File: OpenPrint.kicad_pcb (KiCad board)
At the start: 2 copper layers, 20 x 20 mm, 46 parts, among them IC1 SN74AHCT1G125, IC2 100026223, J1 USB4215-03-A_REVA, U1 RP2354A, U2 AP2112K-3.3, U3 ATECC608C-MAHDA, U4 USBLC6-2SC6, Y1 ABM8-272-T3

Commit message: initial layout done
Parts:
- removed JP1, JP2: Jumper_2_Open, TestPoint:TestPoint_2Pads_Pitch2.54mm_Drill0.8mm
- removed the R12 at (123.0, 59.5)
- added C19: 0.1uF, Capacitor_SMD:C_0402_1005Metric, F.Cu at (98.5, 60.5)
- added D2: WS2812B-2020, LED_SMD:LED_WS2812B-2020_PLCC4_2.0x2.0mm, B.Cu at (99.5, 60.5)
- added H1: MountingHole_Pad, MountingHole:MountingHole_2.2mm_M2_Pad, F.Cu at (100.5, 50.5)
- added H2: MountingHole_Pad, MountingHole:MountingHole_2.2mm_M2_Pad, F.Cu at (119.5, 50.5)
- added H3: MountingHole, MountingHole:MountingHole_2mm, F.Cu at (100.5, 69.5)
- added H4: MountingHole, MountingHole:MountingHole_2mm, F.Cu at (119.5, 69.5)
- added R14: 5.1k, Resistor_SMD:R_0402_1005Metric, B.Cu at (117.5, 54.5)
- added S1: SKRPABE010, SamacSys_Parts:SW_SKRPABE010, B.Cu at (120.5, 56.0)
- added S2: SKRPABE010, SamacSys_Parts:SW_SKRPABE010, B.Cu at (99.5, 56.0)
- C1: renamed from C23; moved to B.Cu
- C10: renamed from C9; moved to B.Cu
- C11, C13, C15, C21, C8, IC1, L1, R1, R13, R2, R3, R4, R5, Y1: moved to B.Cu
- C12: renamed from C10; moved to B.Cu
- C14: renamed from C12; moved to B.Cu
- C16: renamed from C17; moved to B.Cu
- C2: renamed from C3; moved to B.Cu
- C20: renamed from C19; moved to B.Cu
- C3: renamed from C1; moved to B.Cu
- C4: renamed from C2; moved to B.Cu
- C5: renamed from C4; moved to B.Cu
- C6: renamed from C5; moved to B.Cu
- C7: renamed from C6; moved to B.Cu
- C9: renamed from C7; moved to B.Cu
- D1: value WS2812B -> WS2812B-2020; footprint LED_SMD:LED_WS2812B_PLCC4_5.0x5.0mm_P3.2mm -> LED_SMD:LED_WS2812B-2020_PLCC4_2.0x2.0mm; moved to B.Cu
- J1: value USB4215-03-A_REVA -> USB4110; footprint SamacSys_Parts:GCT_USB4215-03-A_REVA -> Connector_USB:USB_C_Receptacle_GCT_USB4110
- R6: renamed from R9; moved to B.Cu
- R7: renamed from R6; moved to B.Cu
- R8: renamed from R7; moved to B.Cu
- R9: renamed from R8; moved to B.Cu
- U1: renamed from U3; moved to B.Cu
- U2: renamed from U1; moved to B.Cu
- U3: renamed from U4; moved to B.Cu
- U4: renamed from U2; moved to B.Cu
- moved R6 37.8 mm to (93.0, 52.0), turned to -90 degrees
- moved U1 30.2 mm to (104.0, 59.0), turned to 90 degrees
- moved U2 25.9 mm to (110.0, 65.0), turned to -90 degrees
- moved R8 25.6 mm to (102.0, 56.5), turned to -90 degrees
- moved R9 25.5 mm to (102.0, 58.5), turned to 90 degrees
- moved C17 25.4 mm to (98.5, 64.0), turned to 90 degrees
- moved IC1 25.0 mm to (100.5, 64.5), turned to 180 degrees
- moved D1 24.9 mm to (120.5, 60.5), turned to 180 degrees
- moved L1 23.9 mm to (103.0, 68.1), turned to -90 degrees
- moved R13 21.6 mm to (102.5, 54.5), turned to -90 degrees
- moved C20 21.4 mm to (115.5, 56.5)
- moved R12 21.3 mm to (118.5, 61.5), turned to -90 degrees
- moved C21 20.5 mm to (115.0, 61.5)
- moved R11 20.4 mm to (118.5, 58.5), turned to 90 degrees
- moved C1 20.3 mm to (106.0, 58.0), turned to 90 degrees
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- renumbered C14 to C17, C16 to C18, R14 to R10, R10 to R11, R11 to R12
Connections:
- D1 pad 1: VBUS -> Net-(D1-DOUT)
- D1 pad 2: unconnected-(D1-DOUT-Pad2) -> GND
- D1 pad 3: GND -> Net-(D1-DIN)
- D1 pad 4: Net-(D1-DIN) -> VBUS
- R1 pad 1: /RST -> /RESET
- R13 pad 1: Net-(J1-CC2) -> Net-(J1-CC1)
- U3 pad 1: /USB-CONN_DP -> /USB-CONN_DM
- U3 pad 3: /USB-CONN_DM -> /USB-CONN_DP
- U3 pad 4: /USB-MCU_DM -> /USB-MCU_DP
- U3 pad 6: /USB-MCU_DP -> /USB-MCU_DM
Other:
- board size 20 x 20 mm -> 25 x 25 mm
- copper layers 2 -> 4

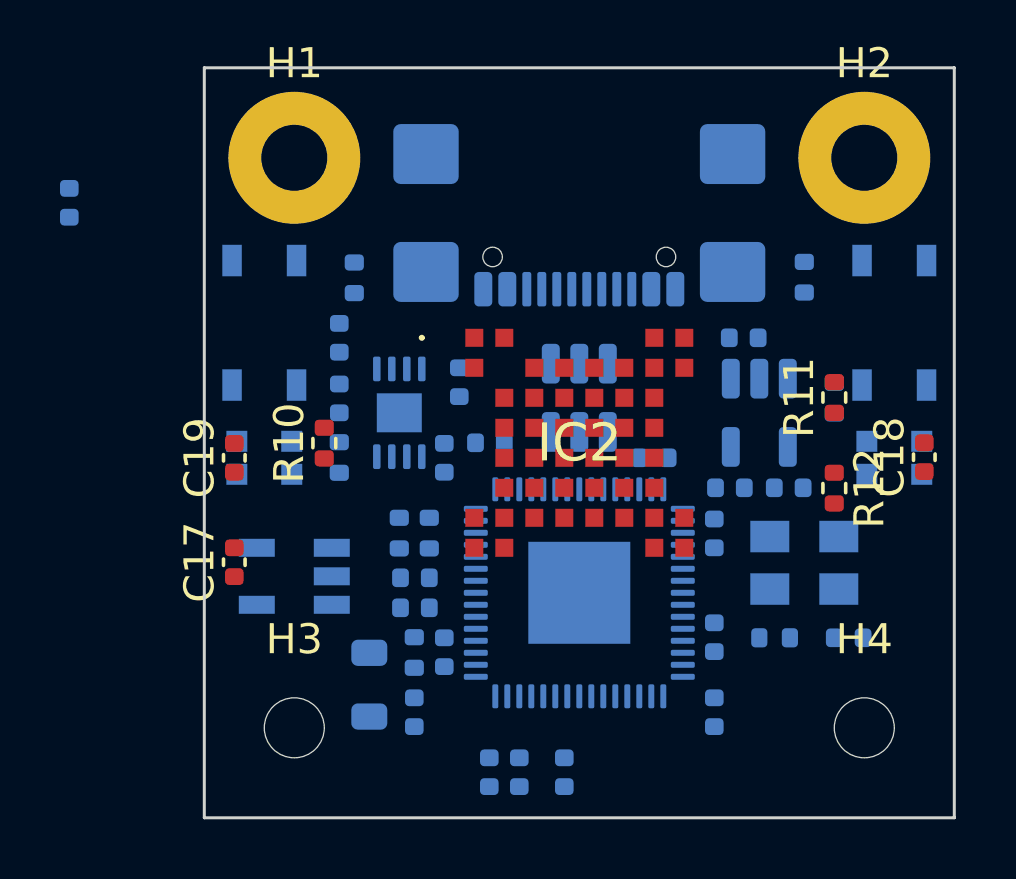
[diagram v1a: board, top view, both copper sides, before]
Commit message: Reposition key SMD parts in PCB layout
Adjusts placement/orientation of multiple 0402 capacitors and resistors, plus nearby parts like the crystal and QFN MCU footprint, to refine routing and spacing in `OpenPrint.kicad_pcb`. Includes KiCad project-local view state update (`active_layer`) and adds two timestamped board backup ZIP archives.
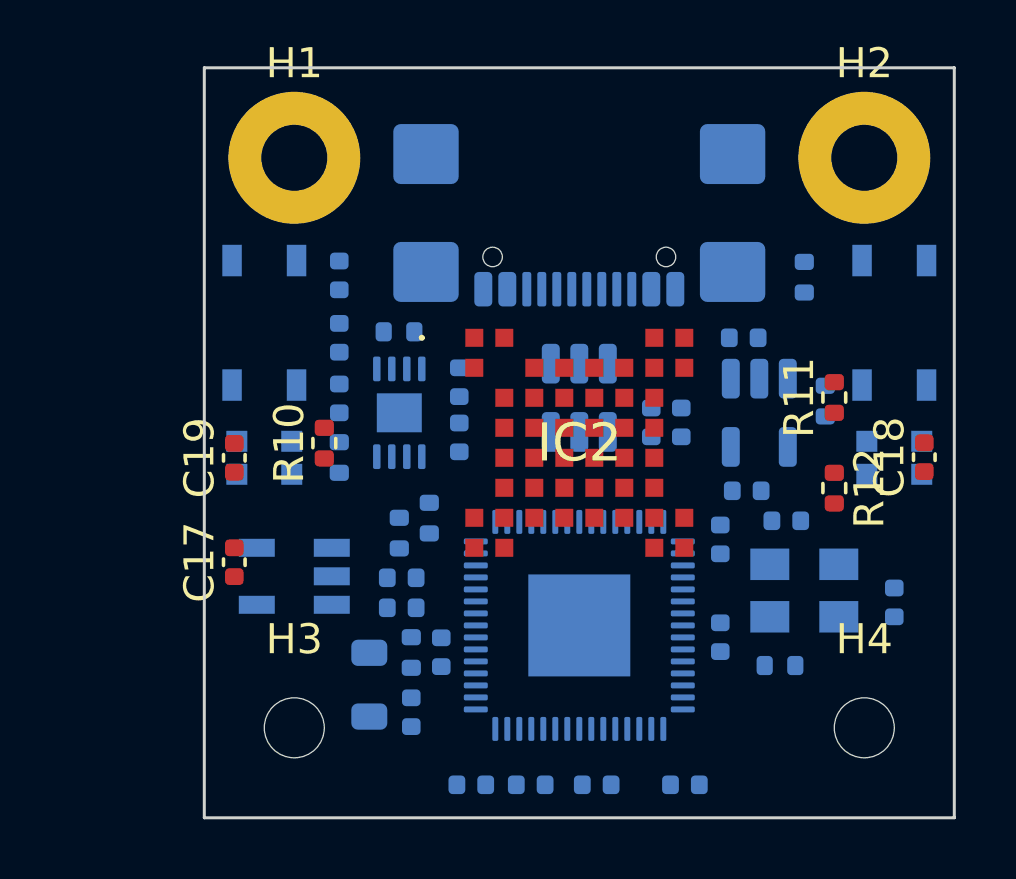
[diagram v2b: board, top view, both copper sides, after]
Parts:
- moved R6 9.32 mm to (102.0, 54.4)
- moved C16 5.42 mm to (112.4, 59.3), turned to 90 degrees
- moved C10 2.61 mm to (113.5, 71.4), turned to 180 degrees
- moved R13 2.34 mm to (104.0, 56.3), turned to 180 degrees
- moved C4 1.92 mm to (120.5, 65.3), turned to 90 degrees
- moved C11 1.50 mm to (113.4, 59.3), turned to 90 degrees
- moved C13 1.16 mm to (110.6, 71.4), turned to 0 degrees
- moved C3 1.10 mm to (116.9, 62.6)
- moved U2 1.09 mm to (110.0, 66.1)
- moved R5 0.94 mm to (116.7, 67.4)
- moved Y1 0.92 mm to (117.5, 64.9)
- moved C6 0.84 mm to (106.0, 59.8)
- moved C7 0.73 mm to (106.4, 71.4), turned to 180 degrees
- moved C21 0.57 mm to (115.6, 61.6), turned to 180 degrees
- moved C8 0.57 mm to (108.4, 71.4), turned to 0 degrees
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
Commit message: Update PCB layout and power routing
Repositions and rearranges PCB footprints, adds back-layer routing and a ground zone, and updates footprint visibility and locking settings. Includes KiCad project metadata and timestamped backup archives.
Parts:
- C17, C18, C19: moved to B.Cu
- moved R10 6.52 mm to (95.1, 58.7)
- moved R12 5.25 mm to (123.7, 60.8)
- moved R11 5.15 mm to (123.7, 58.5)
- moved R7 4.41 mm to (104.5, 71.4), turned to 180 degrees
- moved C17 2.98 mm to (100.9, 62.2), turned to 180 degrees
- moved C14 2.61 mm to (104.4, 68.1), turned to -90 degrees
- moved C18 2.31 mm to (120.1, 62.3), turned to 180 degrees
- moved C19 1.84 mm to (99.1, 62.2), turned to 0 degrees
- moved C9 1.43 mm to (104.5, 70.4), turned to 0 degrees
- moved C12 1.11 mm to (105.4, 68.1)
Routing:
- net /VREG_LX: track 0.00 -> 4.04 mm
- net /VREG_AVDD: track 0.00 -> 3.29 mm
- added copper zone on B.Cu, net GND

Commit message: Route USB D- and update PCB layout
Renames USB D- nets consistently in the schematic and PCB, updates component placement and routing, and adds refined copper zones and fill settings for improved connectivity and clearance.
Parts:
- moved R3 2.41 mm to (104.4, 64.8)
- moved R2 1.91 mm to (103.4, 64.8)
- moved C5 1.39 mm to (105.4, 64.9), turned to 90 degrees
- moved C6 1.33 mm to (107.0, 58.9)
- moved L1 0.36 mm to (102.7, 68.2)
- moved C12 0.36 mm to (105.1, 68.2)
- moved C14 0.36 mm to (104.1, 68.2)
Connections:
- net /USB-CONN_DM renamed /USB-CONN_DN
- net /USB-MCU_DM renamed /USB-MCU_DN
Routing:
- net /USB-MCU_DP: track 0.00 -> 10.00 mm
- net /USB-MCU_DN: track 0.00 -> 8.47 mm
- net /USB-CONN_DP: track 0.00 -> 4.94 mm
- net /USB-CONN_DN: track 0.00 -> 4.29 mm
- net Net-(U2-USB_DM): track 0.00 -> 4.04 mm
- net Net-(U2-USB_DP): track 0.00 -> 2.86 mm
- net +1V1: track 0.00 -> 2.25 mm, vias 0 -> 2
- net /SCL: track 0.00 -> 1.56 mm
- net /SDA: track 0.00 -> 1.38 mm
- net /QSPI_SS: track 0.00 -> 1.04 mm, vias 0 -> 1
- added copper zone on B.Cu, net +1V1
- added copper zone on B.Cu, net +3V3
